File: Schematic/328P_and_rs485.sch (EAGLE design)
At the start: 9 parts, among them IC1 ATMEGA328P

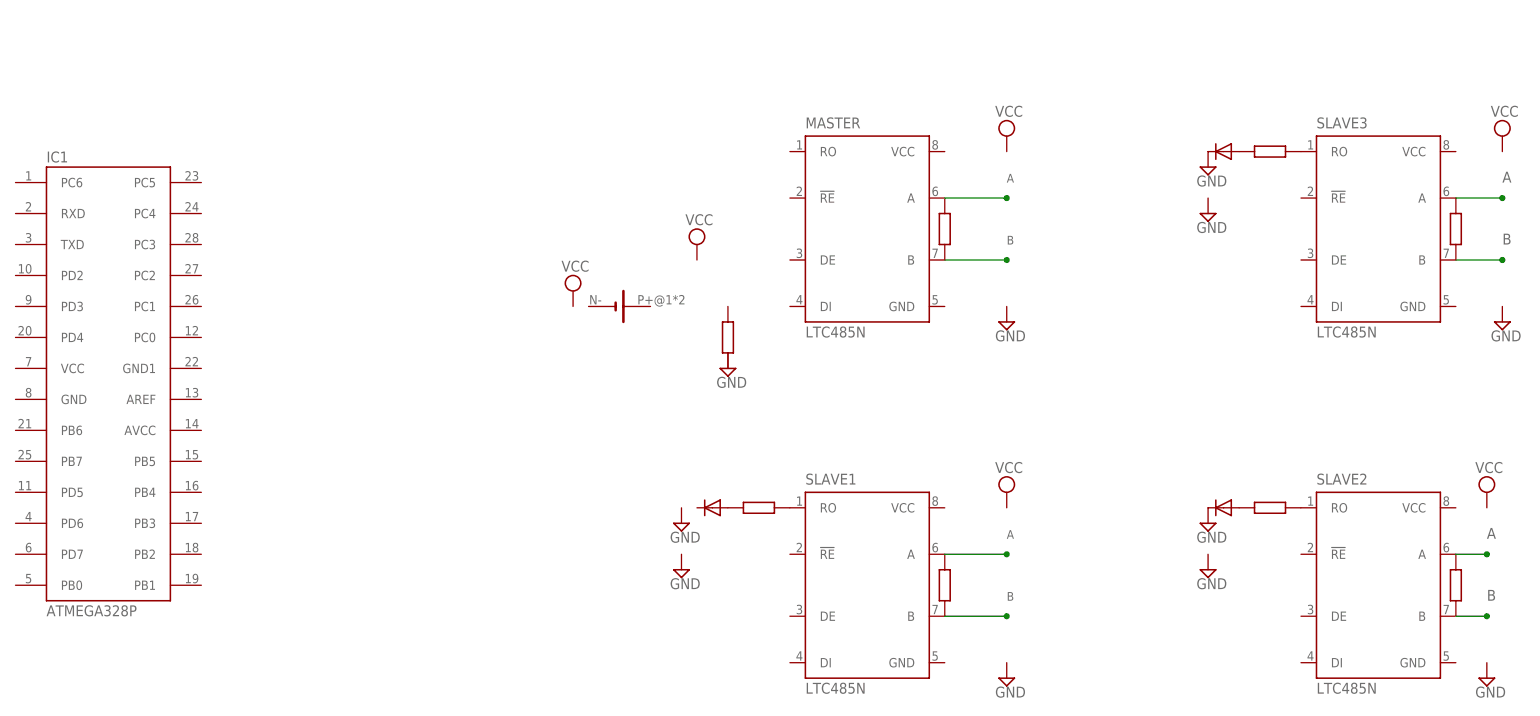
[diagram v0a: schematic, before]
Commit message: 328P and rs485 schematic
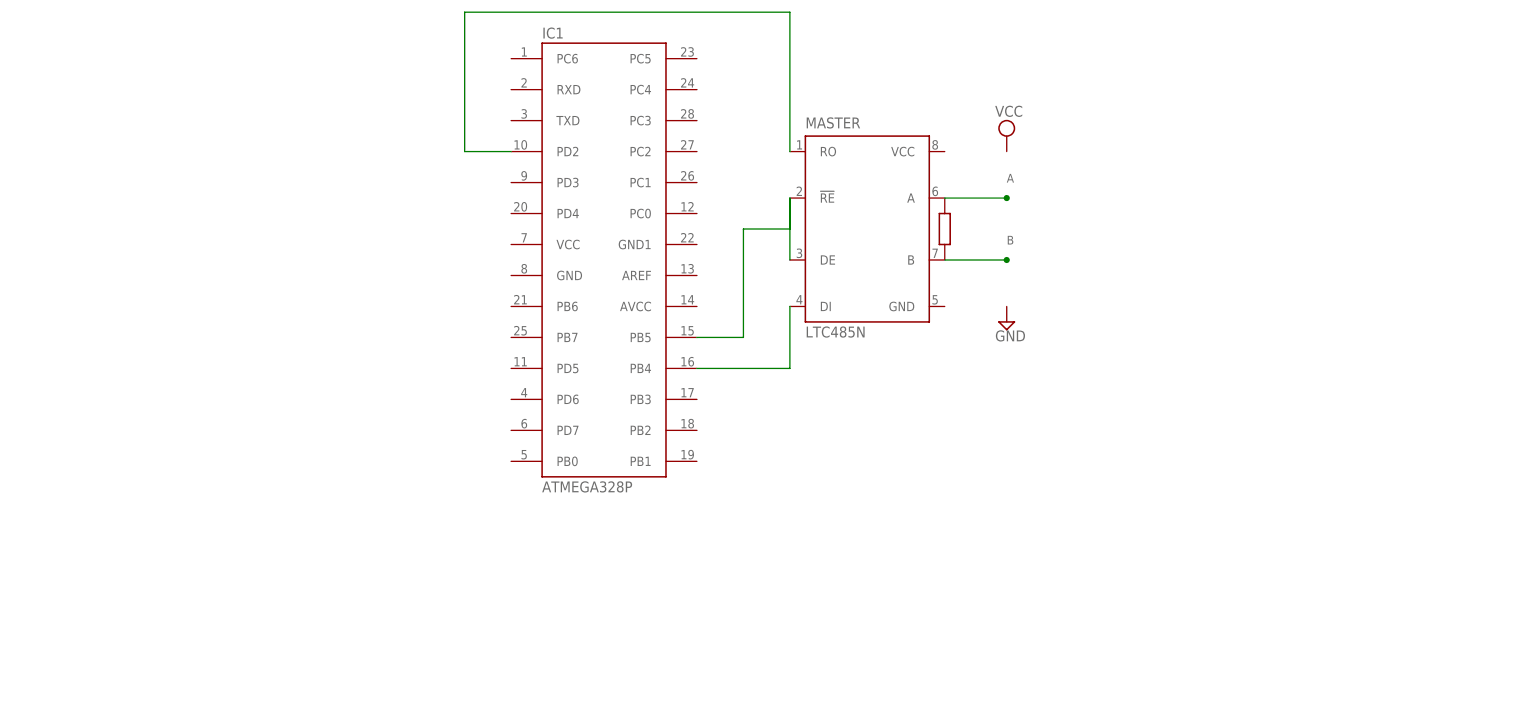
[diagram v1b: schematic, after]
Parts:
- removed D1, D2, D3: 1N4004, diode:1N4004
- removed G1: BATTERY-HOLDER_11.6MM, battery:BATTERY-HOLDER_11.6MM
- removed SLAVE1, SLAVE2, SLAVE3: LTC485N, linear-technology:LTC485N
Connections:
- removed net GND: D2.C, D3.C
- new net N$1: IC1.PB5, MASTER.!RE, MASTER.DE
- new net N$2: IC1.PB4, MASTER.DI
- new net N$3: IC1.PD2, MASTER.RO
- net A: no longer SLAVE1.A, SLAVE2.A, SLAVE3.A
- net B: no longer SLAVE1.B, SLAVE2.B, SLAVE3.B
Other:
- moved on the sheet: IC1
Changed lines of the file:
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@@
 <parts>
 <part name="MASTER" library="linear-technology" deviceset="LTC485" device="N"/>
-<part name="R1" library="docu-dummy" deviceset="R" device=""/>
-<part name="SLAVE1" library="linear-technology" deviceset="LTC485" device="N"/>
 <part name="R2" library="docu-dummy" deviceset="R" device=""/>
-<part name="SUPPLY1" library="supply2" deviceset="VCC" device=""/>
-<part name="SUPPLY2" library="supply2" deviceset="GND" device=""/>
 <part name="SUPPLY3" library="supply2" deviceset="GND" device=""/>
 <part name="SUPPLY4" library="supply2" deviceset="VCC" device=""/>
-<part name="R3" library="docu-dummy" deviceset="R" device=""/>
-<part name="D1" library="diode" deviceset="1N4004" device=""/>
-<part name="SUPPLY5" library="supply2" deviceset="GND" device=""/>
-<part name="SUPPLY6" library="supply2" deviceset="GND" device=""/>
-<part name="SUPPLY7" library="supply2" deviceset="GND" device=""/>
-<part name="R4" library="docu-dummy" deviceset="R" device=""/>
-<part name="SUPPLY8" library="supply2" deviceset="VCC" device=""/>
-<part name="G1" library="battery" deviceset="BATTERY-HOLDER_11.6MM" device=""/>
-<part name="SUPPLY9" library="supply2" deviceset="VCC" device=""/>
-<part name="SLAVE2" library="linear-technology" deviceset="LTC485" device="N"/>
-<part name="SLAVE3" library="linear-technology" deviceset="LTC485" device="N"/>
-<part name="SUPPLY10" library="supply2" deviceset="VCC" device=""/>
-<part name="SUPPLY11" library="supply2" deviceset="GND" device=""/>
-<part name="R5" library="docu-dummy" deviceset="R" device=""/>
-<part name="D2" library="diode" deviceset="1N4004" device=""/>
-<part name="SUPPLY12" library="supply2" deviceset="GND" device=""/>
-<part name="SUPPLY13" library="supply2" deviceset="GND" device=""/>
-<part name="SUPPLY14" library="supply2" deviceset="GND" device=""/>
-<part name="SUPPLY15" library="supply2" deviceset="VCC" device=""/>
-<part name="R6" library="docu-dummy" deviceset="R" device=""/>
-<part name="D3" library="diode" deviceset="1N4004" device=""/>
-<part name="SUPPLY16" library="supply2" deviceset="GND" device=""/>
-<part name="SUPPLY17" library="supply2" deviceset="GND" device=""/>
-<part name="R7" library="docu-dummy" deviceset="R" device=""/>
-<part name="R8" library="docu-dummy" deviceset="R" device=""/>
 <part name="IC1" library="Arduino-AVR" deviceset="ATMEGA328P" device=""/>
 </parts>
@@
 <sheet>
 <plain>
-<wire x1="0" y1="86.36" x2="10.16" y2="86.36" width="0.1524" layer="90"/>
-<wire x1="0" y1="60.96" x2="10.16" y2="60.96" width="0.1524" layer="90"/>
 <wire x1="0" y1="144.78" x2="10.16" y2="144.78" width="0.1524" layer="90"/>
 <wire x1="0" y1="119.38" x2="10.16" y2="119.38" width="0.1524" layer="90"/>
-<wire x1="-40.64" y1="86.36" x2="-43.18" y2="86.36" width="0.1524" layer="90"/>
-<wire x1="-25.4" y1="78.74" x2="-25.4" y2="60.96" width="0.1524" layer="90"/>
-<wire x1="-25.4" y1="78.74" x2="-43.18" y2="78.74" width="0.1524" layer="90"/>
-<wire x1="-25.4" y1="137.16" x2="-25.4" y2="127" width="0.1524" layer="90"/>
-<wire x1="-25.4" y1="127" x2="-40.64" y2="127" width="0.1524" layer="90"/>
-<wire x1="-25.4" y1="119.38" x2="-50.8" y2="119.38" width="0.1524" layer="90"/>
-<wire x1="-58.42" y1="119.38" x2="-60.96" y2="119.38" width="0.1524" layer="90"/>
-<wire x1="83.82" y1="86.36" x2="88.9" y2="86.36" width="0.1524" layer="90"/>
-<wire x1="83.82" y1="60.96" x2="88.9" y2="60.96" width="0.1524" layer="90"/>
-<wire x1="58.42" y1="60.96" x2="58.42" y2="78.74" width="0.1524" layer="90"/>
-<wire x1="58.42" y1="78.74" x2="43.18" y2="78.74" width="0.1524" layer="90"/>
-<wire x1="83.82" y1="144.78" x2="91.44" y2="144.78" width="0.1524" layer="90"/>
-<wire x1="83.82" y1="119.38" x2="91.44" y2="119.38" width="0.1524" layer="90"/>
-<wire x1="58.42" y1="119.38" x2="58.42" y2="137.16" width="0.1524" layer="90"/>
-<wire x1="58.42" y1="137.16" x2="43.18" y2="137.16" width="0.1524" layer="90"/>
 </plain>
 <instances>
 <instance part="MASTER" gate="G$1" x="-12.7" y="134.62"/>
-<instance part="R1" gate="G$1" x="0" y="73.66" rot="R90"/>
-<instance part="SLAVE1" gate="G$1" x="-12.7" y="76.2"/>
 <instance part="R2" gate="G$1" x="0" y="132.08" rot="R90"/>
-<instance part="SUPPLY1" gate="G$1" x="10.16" y="88.9"/>
-<instance part="SUPPLY2" gate="GND" x="10.16" y="58.42"/>
 <instance part="SUPPLY3" gate="GND" x="10.16" y="116.84"/>
 <instance part="SUPPLY4" gate="G$1" x="10.16" y="147.32"/>
-<instance part="R3" gate="G$1" x="-30.48" y="86.36"/>
-<instance part="D1" gate="1" x="-38.1" y="86.36" rot="R180"/>
-<instance part="SUPPLY5" gate="GND" x="-43.18" y="83.82"/>
-<instance part="SUPPLY6" gate="GND" x="-43.18" y="76.2"/>
-<instance part="SUPPLY7" gate="GND" x="-35.56" y="109.22"/>
-<instance part="R4" gate="G$1" x="-35.56" y="114.3" rot="R90"/>
-<instance part="SUPPLY8" gate="G$1" x="-40.64" y="129.54"/>
-<instance part="G1" gate="G$1" x="-53.34" y="119.38"/>
-<instance part="SUPPLY9" gate="G$1" x="-60.96" y="121.92"/>
-<instance part="SLAVE2" gate="G$1" x="71.12" y="76.2"/>
-<instance part="SLAVE3" gate="G$1" x="71.12" y="134.62"/>
-<instance part="SUPPLY10" gate="G$1" x="88.9" y="88.9"/>
-<instance part="SUPPLY11" gate="GND" x="88.9" y="58.42"/>
-<instance part="R5" gate="G$1" x="53.34" y="86.36"/>
-<instance part="D2" gate="1" x="45.72" y="86.36" rot="R180"/>
-<instance part="SUPPLY12" gate="GND" x="43.18" y="83.82"/>
-<instance part="SUPPLY13" gate="GND" x="43.18" y="76.2"/>
-<instance part="SUPPLY14" gate="GND" x="91.44" y="116.84"/>
-<instance part="SUPPLY15" gate="G$1" x="91.44" y="147.32"/>
-<instance part="R6" gate="G$1" x="53.34" y="144.78"/>
-<instance part="D3" gate="1" x="45.72" y="144.78" rot="R180"/>
-<instance part="SUPPLY16" gate="GND" x="43.18" y="142.24"/>
-<instance part="SUPPLY17" gate="GND" x="43.18" y="134.62"/>
-<instance part="R7" gate="G$1" x="83.82" y="73.66" rot="R90"/>
-<instance part="R8" gate="G$1" x="83.82" y="132.08" rot="R90"/>
-<instance part="IC1" gate="1" x="-121.92" y="111.76"/>
+<instance part="IC1" gate="1" x="-40.64" y="132.08"/>
 </instances>
 <busses>
@@
 <label x="10.16" y="139.7" size="1.4224" layer="95"/>
 </segment>
-<segment>
-<pinref part="SLAVE1" gate="G$1" pin="A"/>
-<wire x1="0" y1="78.74" x2="10.16" y2="78.74" width="0.1524" layer="91"/>
-<junction x="10.16" y="78.74"/>
-<label x="10.16" y="81.28" size="1.4224" layer="95"/>
-</segment>
-<segment>
-<pinref part="SLAVE3" gate="G$1" pin="A"/>
-<wire x1="83.82" y1="137.16" x2="91.44" y2="137.16" width="0.1524" layer="91"/>
-<junction x="91.44" y="137.16"/>
-<label x="91.44" y="139.7" size="1.778" layer="95"/>
-</segment>
-<segment>
-<pinref part="SLAVE2" gate="G$1" pin="A"/>
-<wire x1="83.82" y1="78.74" x2="88.9" y2="78.74" width="0.1524" layer="91"/>
-<junction x="88.9" y="78.74"/>
-<label x="88.9" y="81.28" size="1.778" layer="95"/>
-</segment>
 </net>
 <net name="B" class="0">
@@
 <label x="10.16" y="129.54" size="1.4224" layer="95"/>
 </segment>
+</net>
+<net name="N$1" class="0">
 <segment>
-<pinref part="SLAVE1" gate="G$1" pin="B"/>
-<wire x1="0" y1="68.58" x2="10.16" y2="68.58" width="0.1524" layer="91"/>
-<junction x="10.16" y="68.58"/>
-<label x="10.16" y="71.12" size="1.4224" layer="95"/>
-</segment>
-<segment>
-<pinref part="SLAVE3" gate="G$1" pin="B"/>
-<wire x1="83.82" y1="127" x2="91.44" y2="127" width="0.1524" layer="91"/>
-<junction x="91.44" y="127"/>
-<label x="91.44" y="129.54" size="1.778" layer="95"/>
-</segment>
-<segment>
-<pinref part="SLAVE2" gate="G$1" pin="B"/>
-<wire x1="83.82" y1="68.58" x2="88.9" y2="68.58" width="0.1524" layer="91"/>
-<junction x="88.9" y="68.58"/>
-<label x="88.9" y="71.12" size="1.778" layer="95"/>
+<pinref part="IC1" gate="1" pin="PB5"/>
+<wire x1="-40.64" y1="114.3" x2="-33.02" y2="114.3" width="0.1524" layer="91"/>
+<wire x1="-33.02" y1="114.3" x2="-33.02" y2="132.08" width="0.1524" layer="91"/>
+<wire x1="-33.02" y1="132.08" x2="-25.4" y2="132.08" width="0.1524" layer="91"/>
+<pinref part="MASTER" gate="G$1" pin="!RE"/>
+<wire x1="-25.4" y1="132.08" x2="-25.4" y2="137.16" width="0.1524" layer="91"/>
+<pinref part="MASTER" gate="G$1" pin="DE"/>
+<wire x1="-25.4" y1="137.16" x2="-25.4" y2="127" width="0.1524" layer="91"/>
 </segment>
 </net>
-<net name="GND" class="0">
+<net name="N$2" class="0">
 <segment>
-<pinref part="D2" gate="1" pin="C"/>
-<pinref part="SUPPLY12" gate="GND" pin="GND"/>
-</segment>
-<segment>
-<pinref part="D3" gate="1" pin="C"/>
-<pinref part="SUPPLY16" gate="GND" pin="GND"/>
+<pinref part="IC1" gate="1" pin="PB4"/>
+<pinref part="MASTER" gate="G$1" pin="DI"/>
+<wire x1="-40.64" y1="109.22" x2="-25.4" y2="109.22" width="0.1524" layer="91"/>
+<wire x1="-25.4" y1="109.22" x2="-25.4" y2="119.38" width="0.1524" layer="91"/>
 </segment>
 </net>
+<net name="N$3" class="0">
+<segment>
+<pinref part="IC1" gate="1" pin="PD2"/>
+<wire x1="-71.12" y1="144.78" x2="-78.74" y2="144.78" width="0.1524" layer="91"/>
+<wire x1="-78.74" y1="144.78" x2="-78.74" y2="167.64" width="0.1524" layer="91"/>
+<pinref part="MASTER" gate="G$1" pin="RO"/>
+<wire x1="-78.74" y1="167.64" x2="-25.4" y2="167.64" width="0.1524" layer="91"/>
+<wire x1="-25.4" y1="167.64" x2="-25.4" y2="144.78" width="0.1524" layer="91"/>
+</segment>
+</net>
